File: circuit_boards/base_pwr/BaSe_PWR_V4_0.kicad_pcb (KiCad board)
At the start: 2 copper layers, 89 parts, among them J2 USB_B_Micro, J4 Screw_Terminal_01x04, J5 MOTOR, J6 USB3_B_Micro, J7 USB_C_Receptacle, J8 Screw_Terminal_01x03, J9 USB3_A, P1 USB_C_Plug, Q2 BSS214NW, Q3 BSS214NW, Q4 BSS214NW, Q5 BSS214NW, U2 AMS1117-3.3, U3 STM32F070RBTx, U4 LM2596S-5, U5 DRV8220, U6 AMS1117-3.3, Y1 32.768kHz, Y2 8MHz

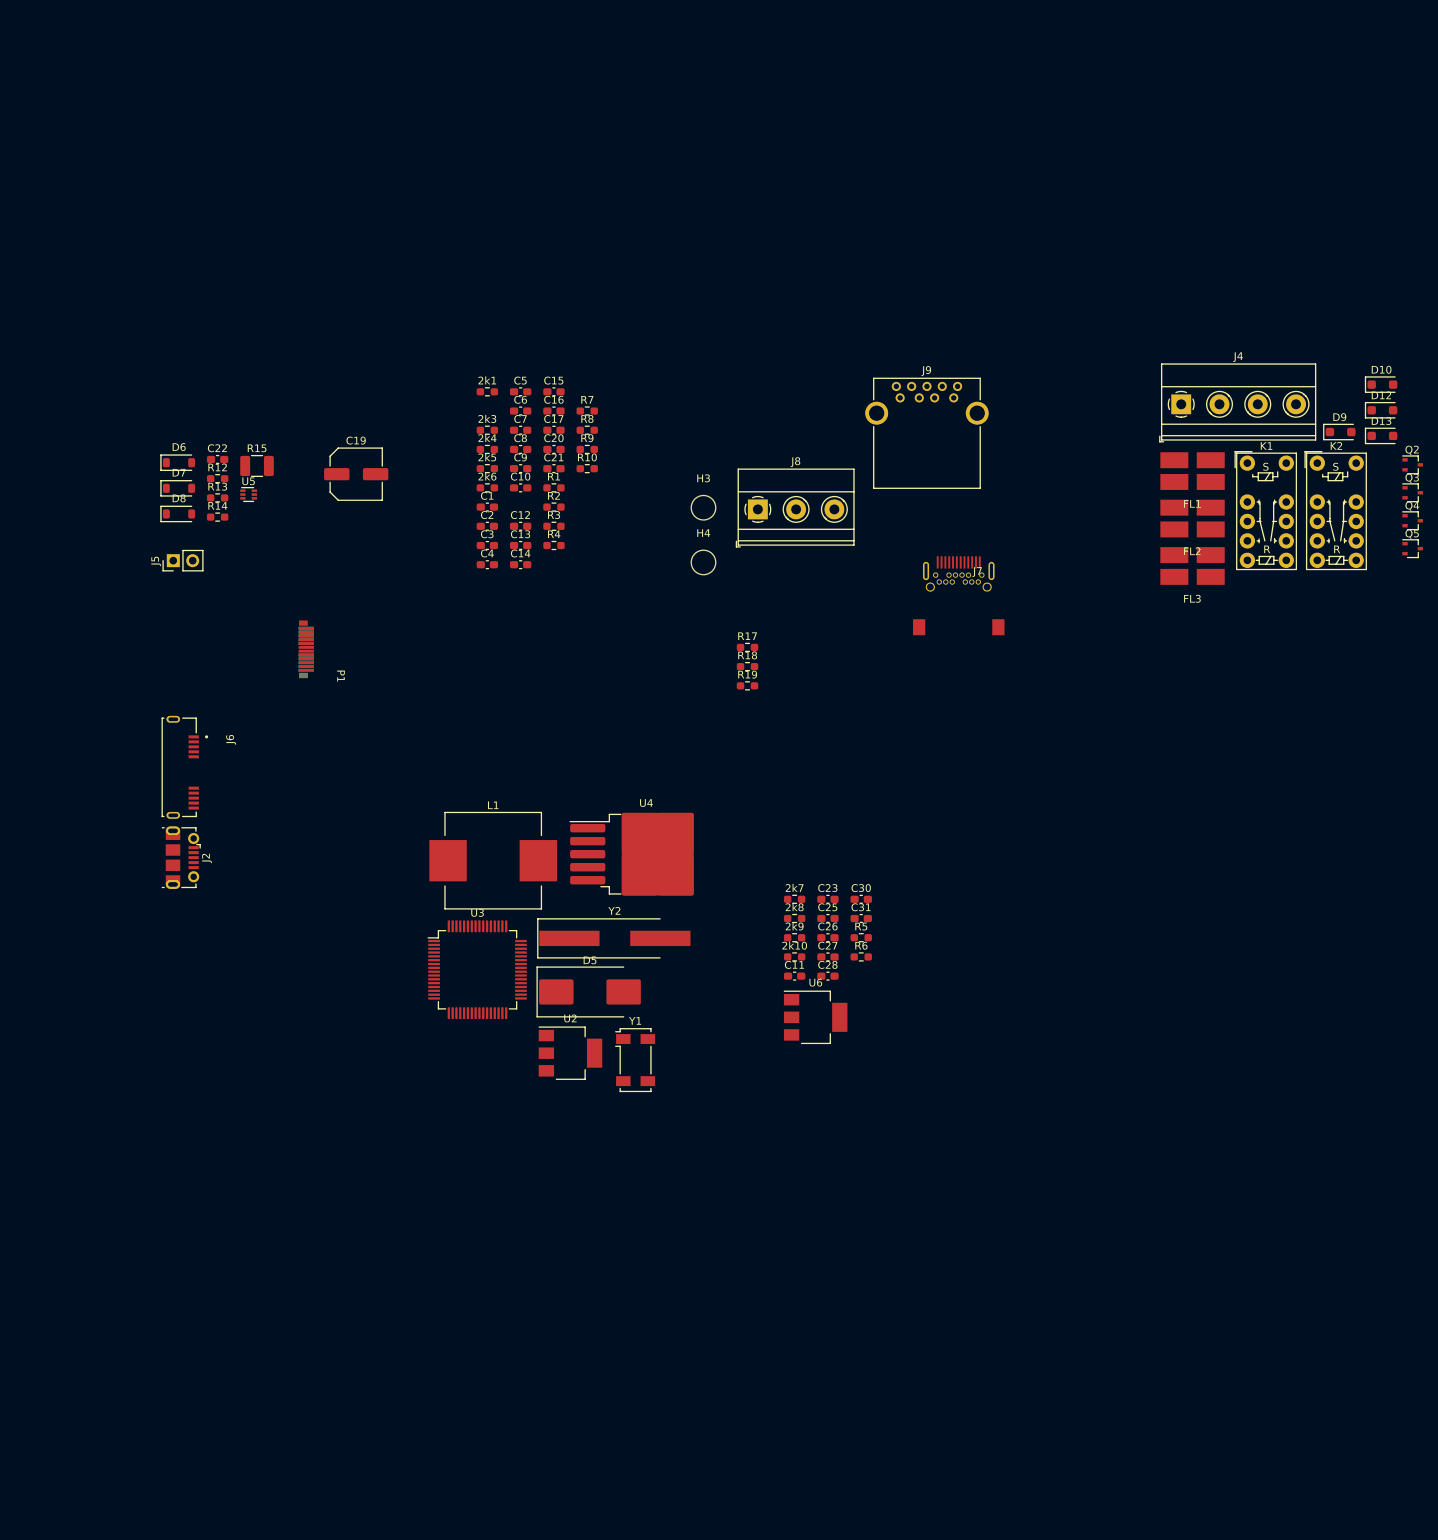
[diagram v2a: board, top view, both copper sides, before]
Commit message: BaSe PWR V4.0: more layout sketches
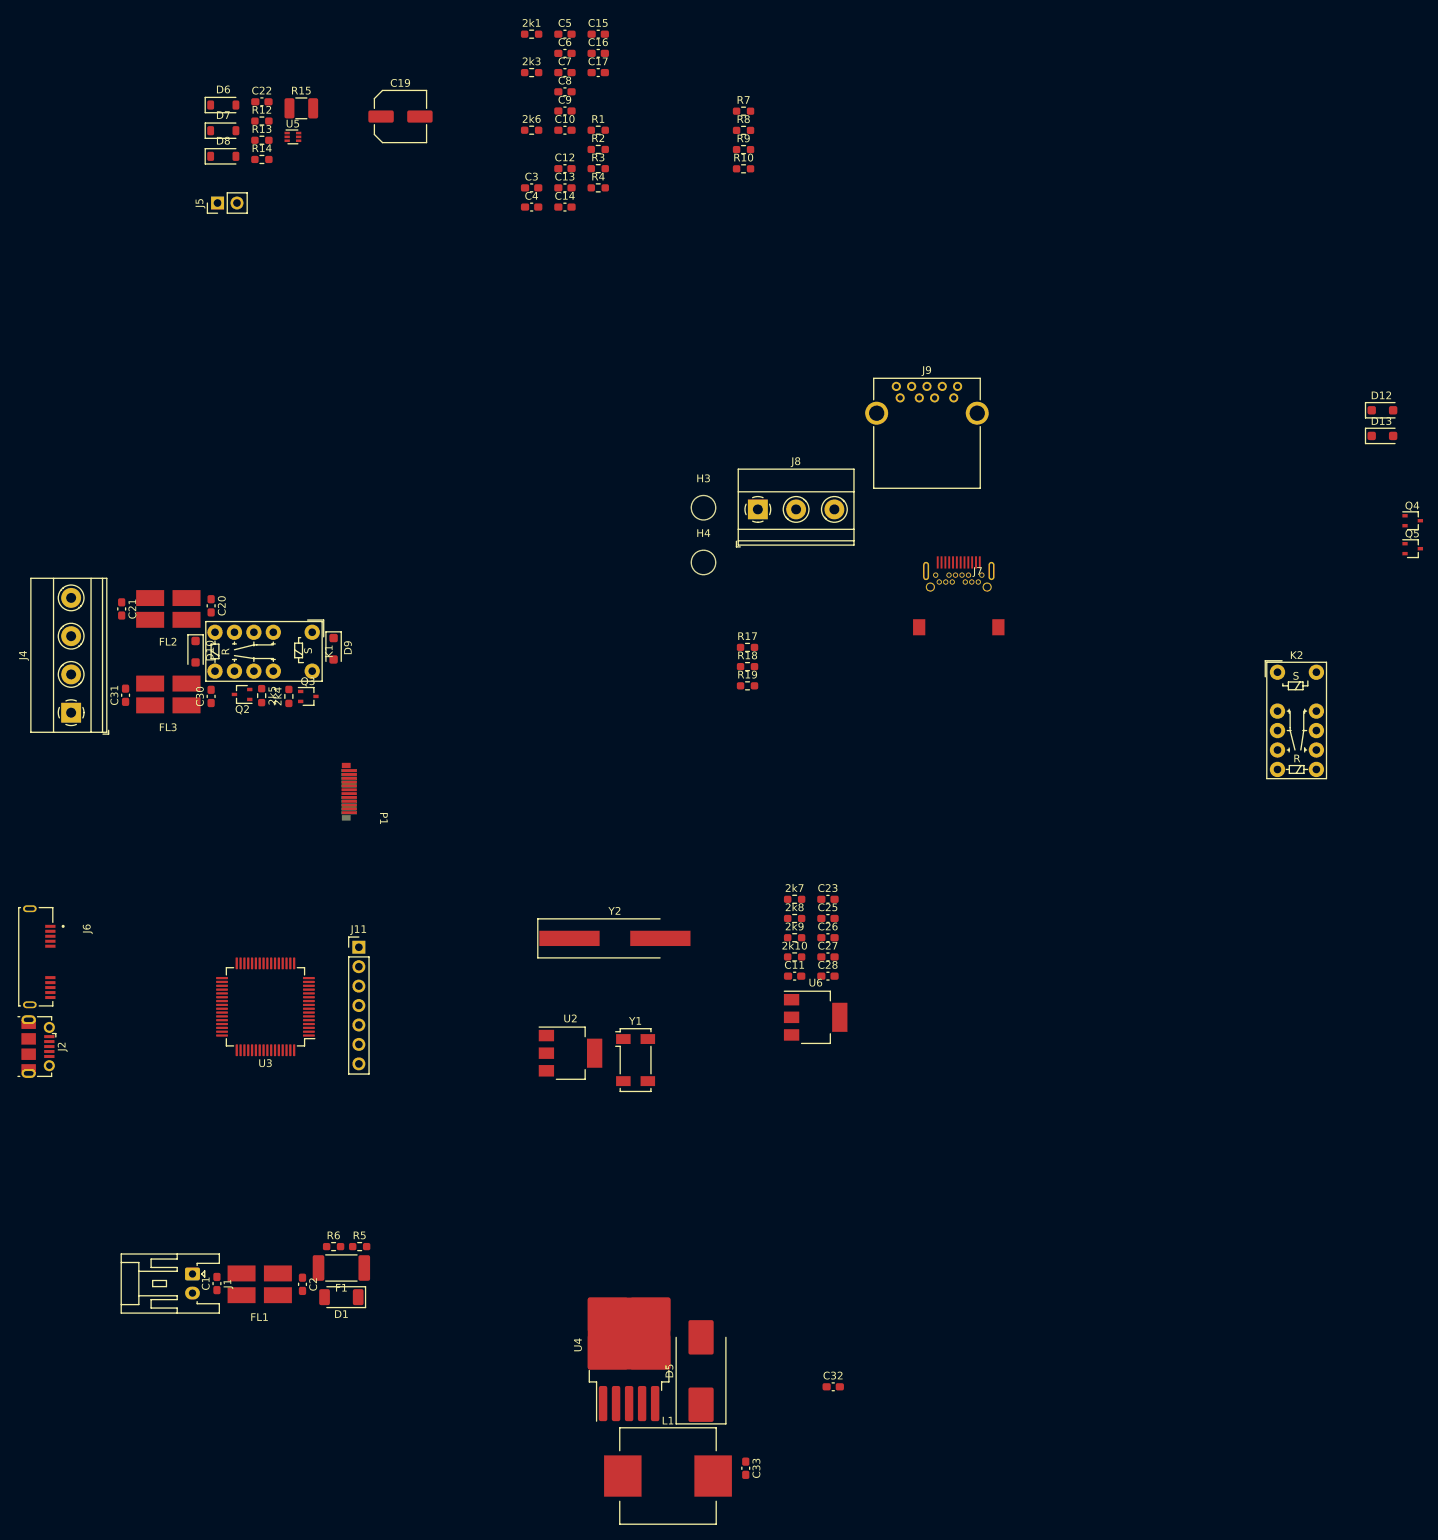
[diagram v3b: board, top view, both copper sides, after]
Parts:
- added C32: ~, Capacitor_SMD:C_0603_1608Metric_Pad1.08x0.95mm_HandSolder, F.Cu at (141.2, 152.9)
- added C33: 100nF, Capacitor_SMD:C_0603_1608Metric_Pad1.08x0.95mm_HandSolder, F.Cu at (129.8, 163.6)
- added D1: ~, Diode_SMD:D_SOD-128, F.Cu at (77.0, 141.2)
- added F1: ~, Fuse:Fuse_2512_6332Metric_Pad1.52x3.35mm_HandSolder, F.Cu at (77.0, 137.4)
- added J1: 12VDC In, Connector_JST:JST_XA_S02B-XASK-1N-BN_1x02_P2.50mm_Horizontal, F.Cu at (57.5, 138.2)
- added J11: Conn_01x07_Pin, Connector_PinHeader_2.54mm:PinHeader_1x07_P2.54mm_Vertical, F.Cu at (79.2, 95.5)
- C14: value ~ -> 220µF
- C17: value ~ -> 100nF
- moved FL1 161.7 mm to (66.3, 139.5)
- moved D10 158.9 mm to (57.9, 56.9), turned to -90 degrees
- moved Q2 155.9 mm to (64.0, 62.5), turned to 180 degrees
- moved J4 150.5 mm to (41.7, 64.9), turned to 90 degrees
- moved Q3 146.7 mm to (72.6, 62.7)
- moved FL3 134.9 mm to (54.4, 62.5)
- moved D9 134.6 mm to (75.9, 56.5), turned to -90 degrees
- moved FL2 134.3 mm to (54.4, 51.3)
- moved K1 124.2 mm to (73.2, 54.4), turned to -90 degrees
- moved C1 107.4 mm to (60.7, 139.4), turned to 90 degrees
- moved C2 101.9 mm to (71.9, 139.5), turned to -90 degrees
- moved C31 100.4 mm to (48.8, 62.6), turned to 90 degrees
- moved C30 89.0 mm to (59.9, 62.7), turned to 90 degrees
- moved L1 83.6 mm to (119.6, 164.6)
- moved R6 78.6 mm to (75.9, 134.6)
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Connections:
- FL2 pad 1: /+5v_sbu_flt_gnd -> /+5v_sbu_flt
- FL2 pad 2: /+5v_sbu_flt -> /+5v_sbu_flt_gnd
- FL2 pad 3: /+5V_sbu -> GND
- FL2 pad 4: GND -> /+5V_sbu

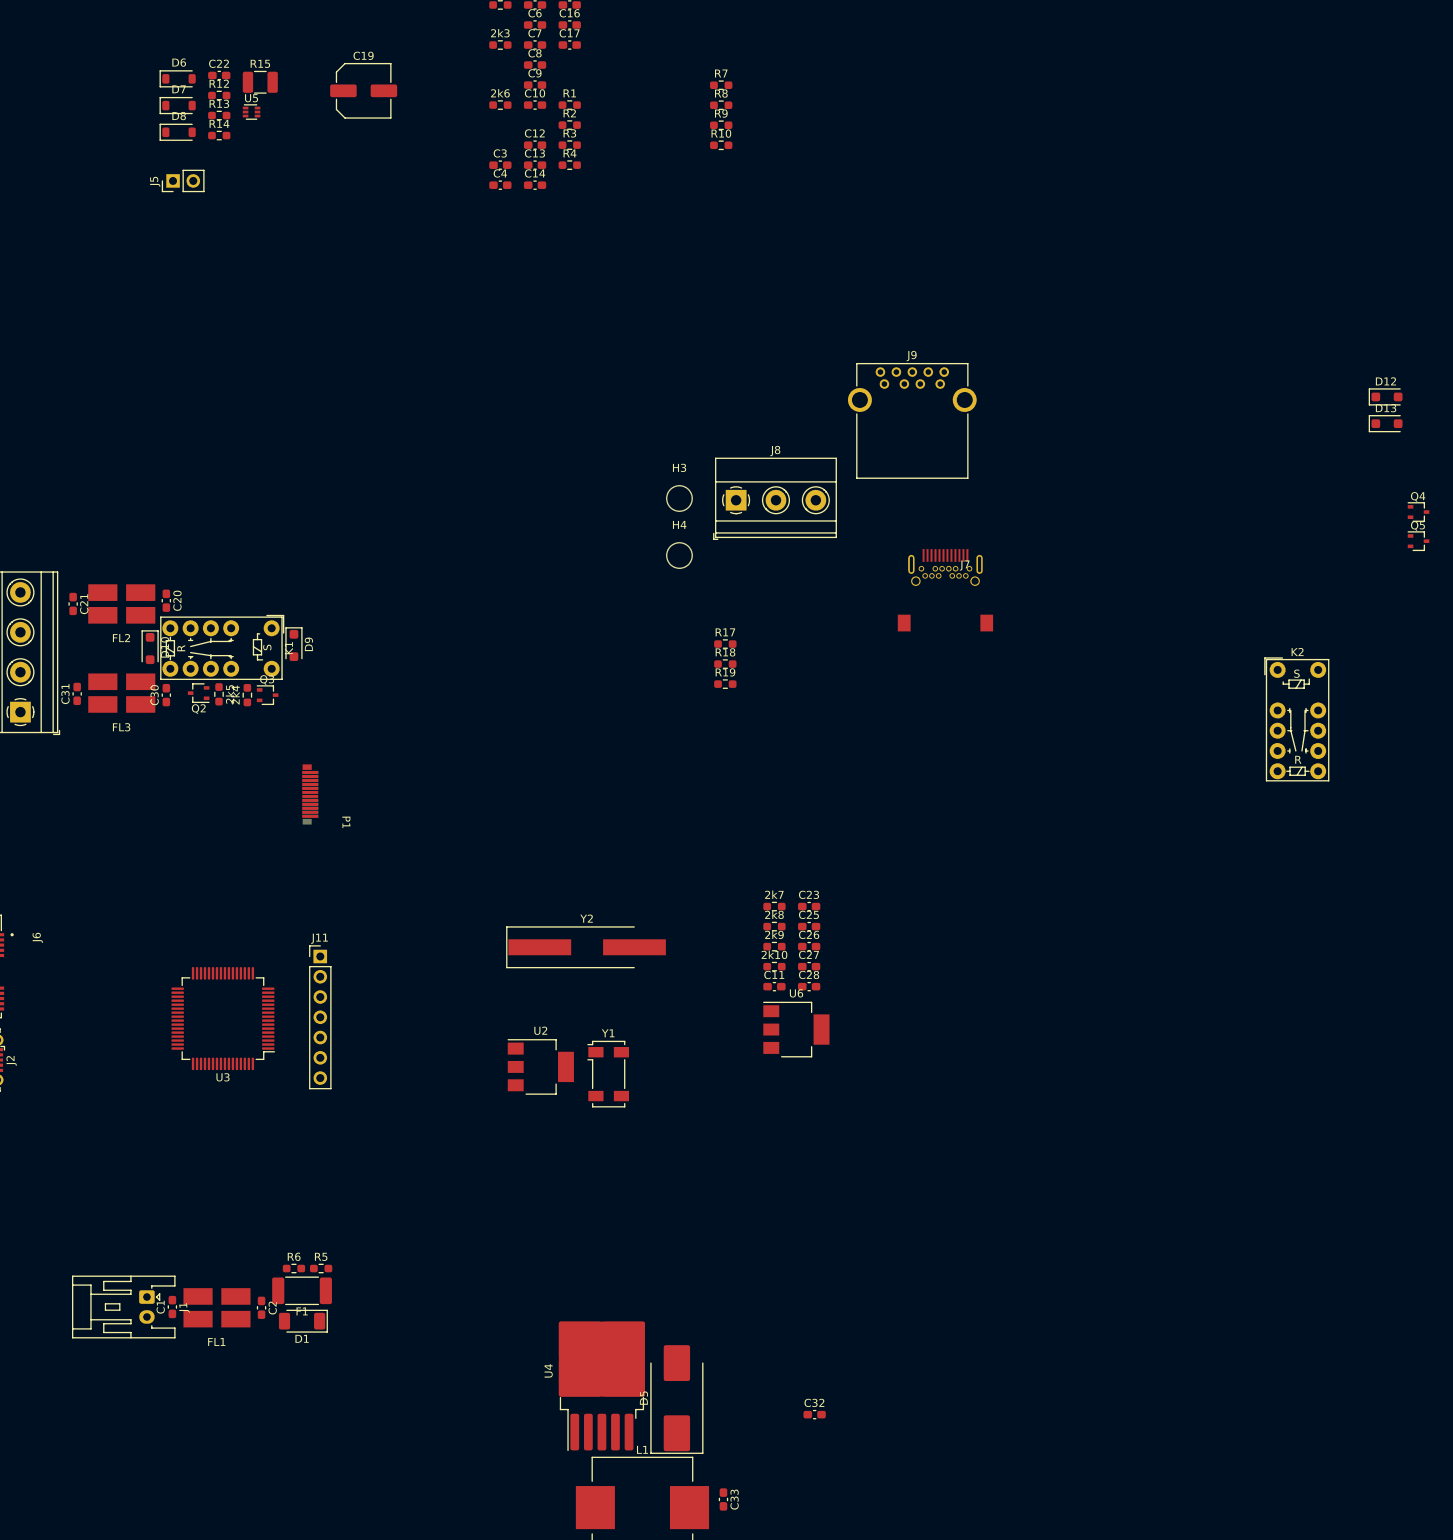
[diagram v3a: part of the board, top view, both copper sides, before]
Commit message: BaSe PWR V4.0: design reverse polarity protection
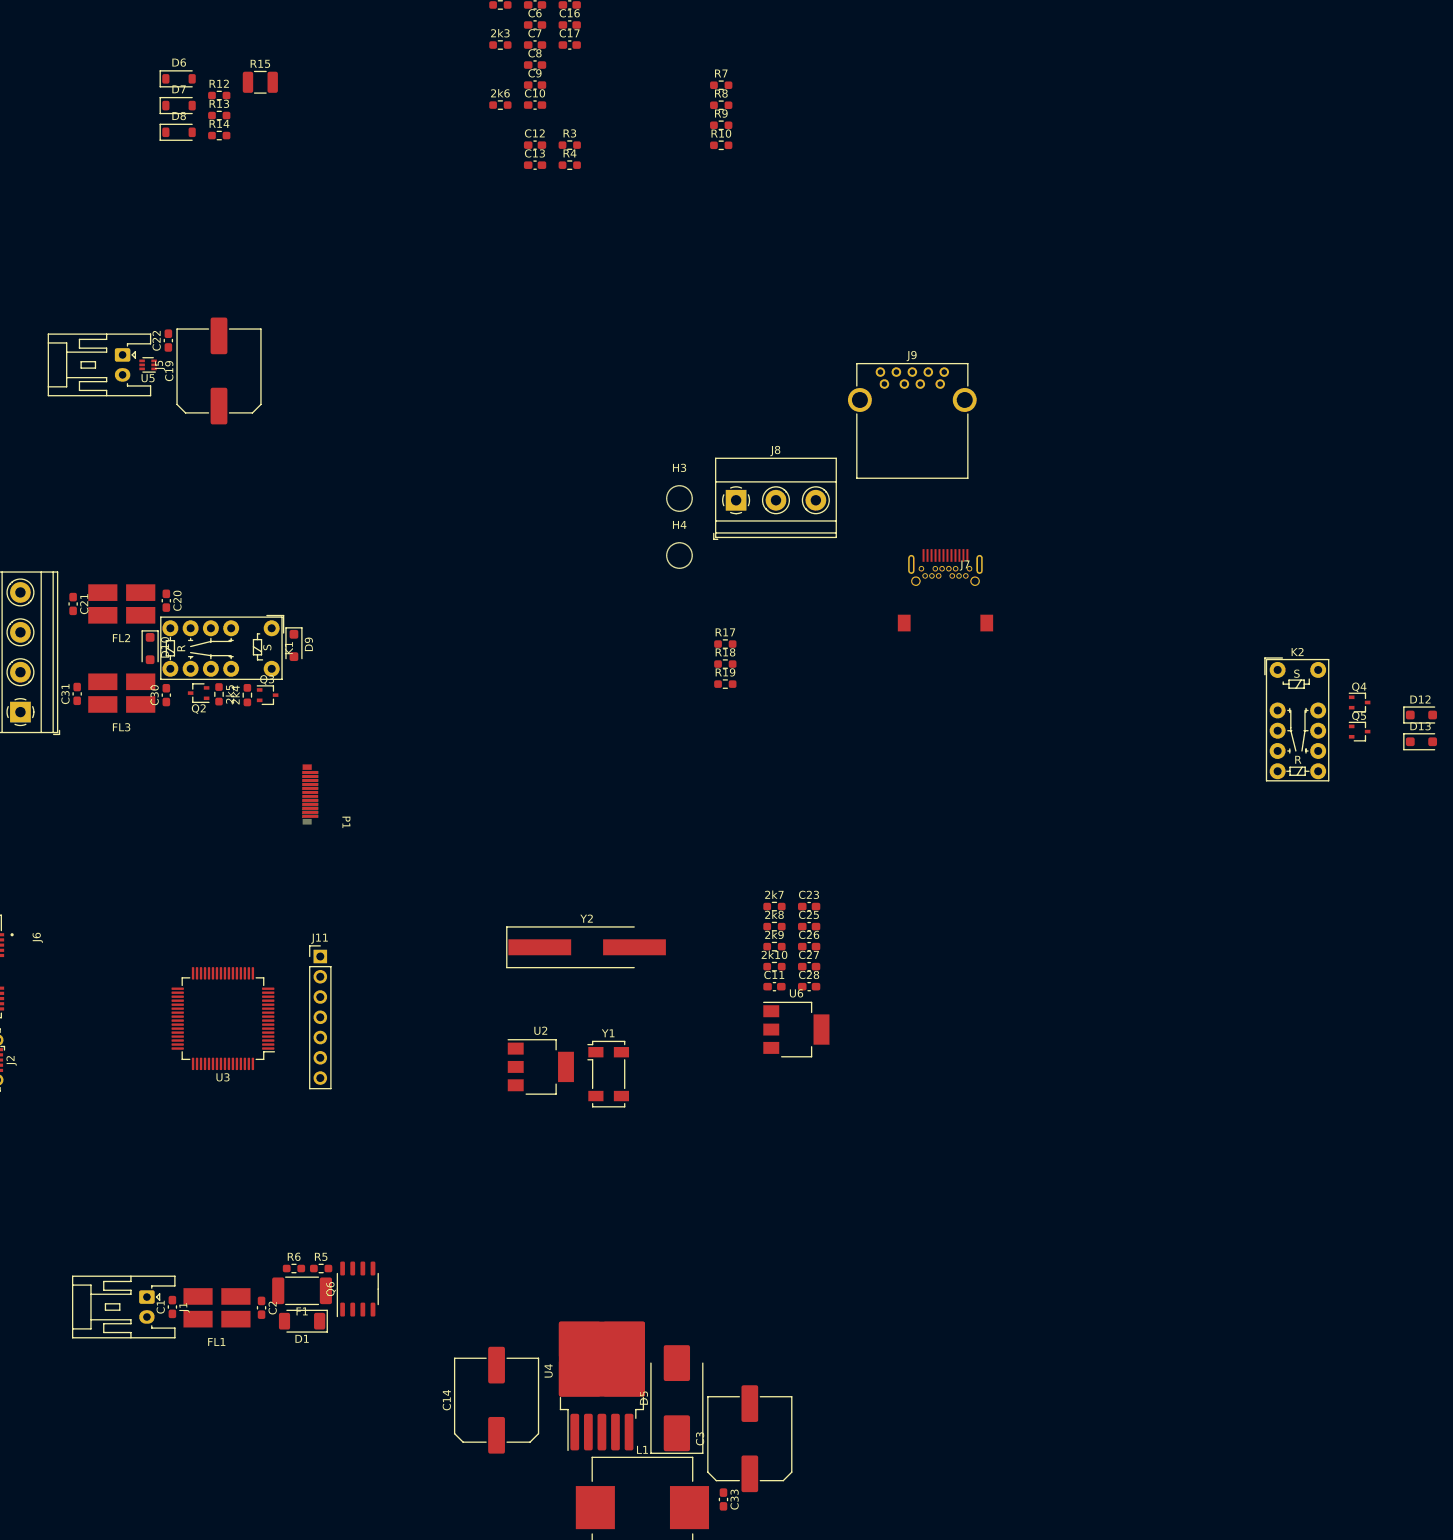
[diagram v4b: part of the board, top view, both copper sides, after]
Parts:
- removed C32, C4: ~, Capacitor_SMD:C_0603_1608Metric_Pad1.08x0.95mm_HandSolder
- removed R1, R2: ~, Resistor_SMD:R_0603_1608Metric_Pad0.98x0.95mm_HandSolder
- added Q6: AOSP21321, Package_SO:SO-8_3.9x4.9mm_P1.27mm, F.Cu at (83.9, 137.2)
- C14: footprint Capacitor_SMD:C_0603_1608Metric_Pad1.08x0.95mm_HandSolder -> Capacitor_SMD:C_Elec_10x10.2
- C19: footprint Capacitor_SMD:C_Elec_6.3x7.7 -> Capacitor_SMD:C_Elec_10x10.2
- C3: value ~ -> 220µF; footprint Capacitor_SMD:C_0603_1608Metric_Pad1.08x0.95mm_HandSolder -> Capacitor_SMD:C_Elec_10x10.2
- D1: value ~ -> 824501121
- J5: footprint Connector_PinHeader_2.54mm:PinHeader_1x02_P2.54mm_Vertical -> Connector_JST:JST_XA_S02B-XASK-1N-BN_1x02_P2.50mm_Horizontal
- moved C3 162.7 mm to (133.1, 156.0), turned to 90 degrees
- moved C14 152.4 mm to (101.3, 151.1), turned to 90 degrees
- moved D12 40.1 mm to (217.3, 65.2)
- moved D13 40.1 mm to (217.3, 68.6)
- moved C19 39.5 mm to (66.5, 22.1), turned to 90 degrees
- moved U5 34.3 mm to (57.7, 21.3), turned to 180 degrees
- moved C22 33.8 mm to (60.2, 18.3), turned to 90 degrees
- moved Q4 25.0 mm to (209.6, 63.7)
- moved Q5 25.0 mm to (209.6, 67.3)
- moved J5 22.7 mm to (54.5, 20.1), turned to -90 degrees
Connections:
- C3 pad 1: +12V -> +5V
- C3 pad 2: Net-(D3-K) -> GND
- R9 pad 1: +3V3_STBY -> /~{LM2596S_ON}
- R9 pad 2: /~{LM2596S_ON} -> GND
- U5 pad 4: Net-(J5-Pin_2) -> Net-(J5-Pin_1)
- U5 pad 6: Net-(J5-Pin_1) -> Net-(J5-Pin_2)

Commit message: BaSe PWR V4.0: settle on rough component distribution
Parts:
- removed C20, C21, C30, C31: ~, Capacitor_SMD:C_0603_1608Metric_Pad1.08x0.95mm_HandSolder
- removed FL2, FL3: ~, g7_emi:CMC_Laird_CM2021Y330R-10
- removed J4: Screw_Terminal_01x04, TerminalBlock_Phoenix:TerminalBlock_Phoenix_MKDS-1,5-4_1x04_P5.00mm_Horizontal
- added J10: Conn_01x04_Socket, Connector_JST:JST_XH_B4B-XH-A_1x04_P2.50mm_Vertical, F.Cu at (95.0, 138.0)
- J1, J5: footprint Connector_JST:JST_XA_S02B-XASK-1N-BN_1x02_P2.50mm_Horizontal -> Connector_JST:JST_XH_B2B-XH-A_1x02_P2.50mm_Vertical
- J6: moved to B.Cu
- moved J7 184.7 mm to (342.3, 44.4)
- moved J8 184.7 mm to (316.0, 35.9)
- moved H3 184.7 mm to (308.9, 35.6)
- moved H4 184.7 mm to (308.9, 42.8)
- moved J9 184.7 mm to (338.1, 19.8)
- moved R17 184.7 mm to (314.7, 53.9)
- moved R18 184.7 mm to (314.7, 56.4)
- moved R19 184.7 mm to (314.7, 58.9)
- moved C5 182.0 mm to (213.1, 123.5), turned to 90 degrees
- moved C6 174.3 mm to (213.1, 116.4), turned to -90 degrees
- moved R3 162.6 mm to (213.1, 120.0), turned to 90 degrees
- moved K2 129.3 mm to (83.9, 118.0), turned to 90 degrees
- moved C17 115.2 mm to (101.7, 96.1), turned to 90 degrees
- moved Y1 109.5 mm to (223.7, 126.1)
- moved 2k1 109.3 mm to (163.2, 66.7)
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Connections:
- net /USB_DM renamed /USB_D-
- net /USB_DP renamed /USB_D+
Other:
- board outline added: 78 x 65 mm
